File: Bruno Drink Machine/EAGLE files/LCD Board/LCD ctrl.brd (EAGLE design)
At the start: 88.2 x 81.2 mm, 38 parts, among them IC1 PIC24FJ256DA210-I/PT, IC2 IS62LV256AL, IC3 IS62LV256AL, IC4 BA3259H-HRP5, P1 CONN-40P-62684-401100ALF, P18 CONN-8P-PND, P2 USB-CON690-005-299-043

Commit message: made some of the changes; not all (will need to go through change list and confirm later)
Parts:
- moved U$32 78.4 mm to (5.08, 83.2), turned to 90 degrees
- moved U$35 78.4 mm to (76.2, 83.2), turned to 90 degrees
- moved U$33 71.1 mm to (5.08, 5.08), turned to 90 degrees
- moved U$34 71.1 mm to (76.2, 5.08), turned to 90 degrees
- moved P2 67.9 mm to (57.7, 85.5), turned to 180 degrees
- moved U$36 61.8 mm to (75.2, 14.0), turned to 90 degrees
- moved P18 57.6 mm to (74.2, 63.8), turned to 90 degrees
- moved P1 51.0 mm to (36.1, 76.4), turned to 180 degrees
- moved U$20 47.1 mm to (68.2, 22.0), turned to 90 degrees
- moved FET1 43.5 mm to (49.3, 70.1), turned to 0 degrees
- moved IC4 43.3 mm to (69.1, 52.0), turned to 270 degrees
- moved IC3 39.0 mm to (18.3, 24.4), turned to 180 degrees
- moved IC2 38.5 mm to (18.3, 56.1), turned to 180 degrees
- moved R2 34.2 mm to (60.2, 54.8), turned to 270 degrees
- moved ICSP1 32.6 mm to (59.2, 27.0), turned to 45 degrees
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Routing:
- net N$6: track 7.28 -> 6.56 mm
- net PGC: track 24.8 -> 24.2 mm
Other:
- board size 88.2 x 81.2 mm -> 81.2 x 88.2 mm

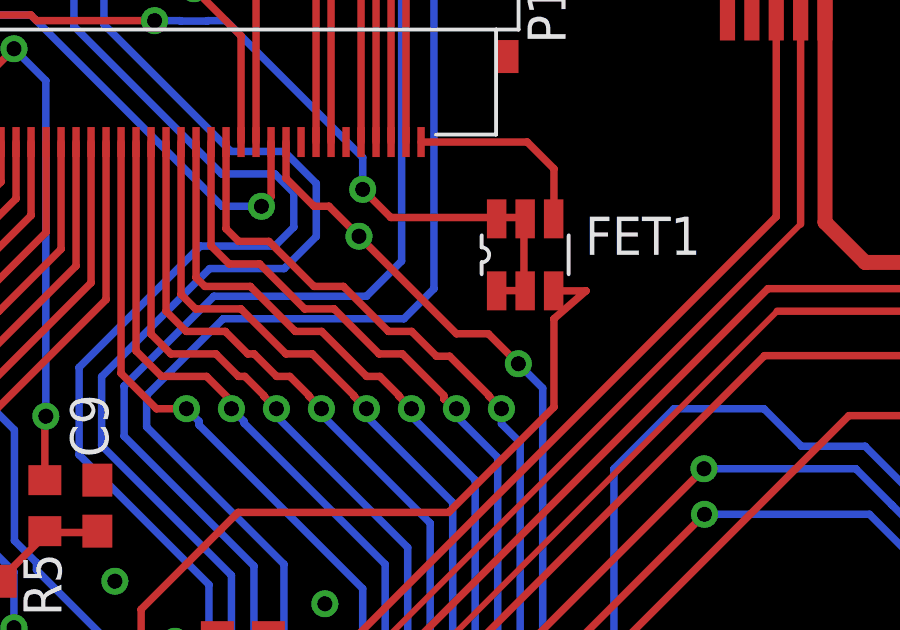
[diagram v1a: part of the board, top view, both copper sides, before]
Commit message: added another change (40p connector wrong) in change log; wrote some code
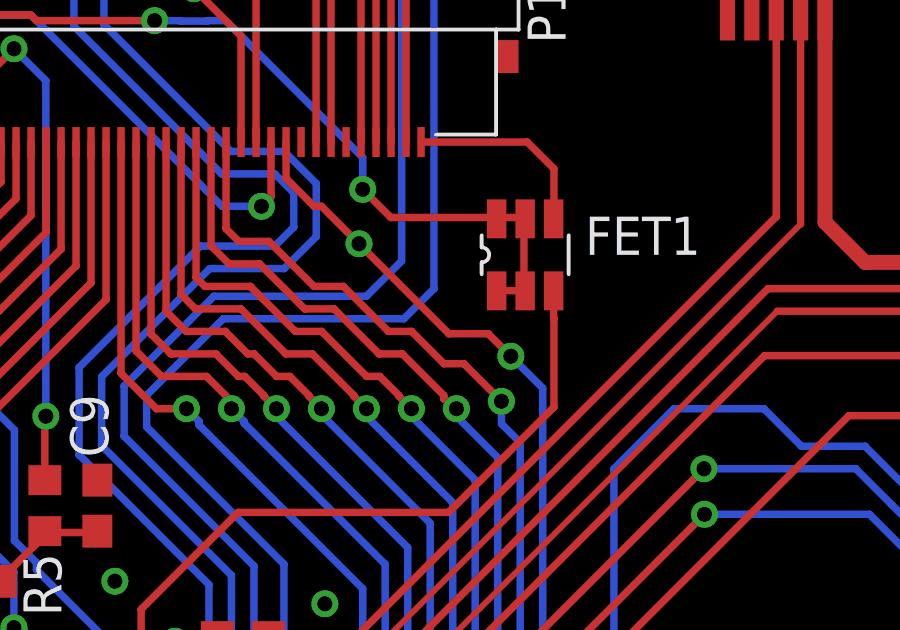
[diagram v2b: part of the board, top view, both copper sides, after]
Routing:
- net BACKLIGHT: track 28.8 -> 27.2 mm
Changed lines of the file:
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@@
 <wire x1="47.3282" y1="18.55339375" x2="47.3282" y2="18.6718" width="0.25" layer="1"/>
 <wire x1="47.3282" y1="18.6718" x2="47.6564" y2="19" width="0.25" layer="1"/>
-<via x="48.5" y="65" extent="1-16" drill="0.5"/>
-<wire x1="48.0782" y1="65.4218" x2="48.0782" y2="65.44660625" width="0.25" layer="1"/>
-<wire x1="48.0782" y1="65.4218" x2="48.5" y2="65" width="0.25" layer="1"/>
-<wire x1="48.5" y1="64.5" x2="48.5" y2="65" width="0.25" layer="16"/>
+<via x="48.5" y="65.25" extent="1-16" drill="0.5"/>
+<wire x1="48.5" y1="64.5" x2="48.5" y2="65.25" width="0.25" layer="16"/>
 <via x="28.75" y="44" extent="1-16" drill="0.5"/>
 <wire x1="47.6564" y1="19" x2="47.6564" y2="17.4064" width="0.25" layer="16"/>
@@
 <wire x1="49.125" y1="30.2434125" x2="49.125" y2="63.875" width="0.25" layer="16"/>
 <wire x1="49.125" y1="63.875" x2="48.5" y2="64.5" width="0.25" layer="16"/>
-<wire x1="48.0782" y1="65.44660625" x2="46.77480625" y2="66.75" width="0.25" layer="1"/>
 <wire x1="45.50726875" y1="67.5782" x2="44.7324625" y2="67.5782" width="0.25" layer="1"/>
-<wire x1="46.77480625" y1="66.75" x2="46.33546875" y2="66.75" width="0.25" layer="1"/>
-<wire x1="46.33546875" y1="66.75" x2="45.50726875" y2="67.5782" width="0.25" layer="1"/>
+<wire x1="46.58546875" y1="66.5" x2="45.50726875" y2="67.5782" width="0.25" layer="1"/>
 <wire x1="44.7324625" y1="67.5782" x2="43.2324625" y2="69.0782" width="0.25" layer="1"/>
 <wire x1="43.2324625" y1="69.0782" x2="42.24991875" y2="69.0782" width="0.25" layer="1"/>
@@
 <wire x1="39.32" y1="73.89" x2="39.32" y2="71" width="0.25" layer="1"/>
 <wire x1="39.32" y1="71" x2="39.7418" y2="70.5782" width="0.25" layer="1"/>
+<wire x1="48.5" y1="65.25" x2="47.25" y2="66.5" width="0.25" layer="1"/>
+<wire x1="47.25" y1="66.5" x2="46.58546875" y2="66.5" width="0.25" layer="1"/>
 </signal>
 <signal name="DB1">
@@
 <contactref element="P1" pad="31"/>
 <wire x1="41.32" y1="73.89" x2="41.32" y2="72.68" width="0.25" layer="1"/>
-<via x="43.75" y="70.75" extent="1-16" drill="0.5"/>
+<via x="43.75" y="70.5" extent="1-16" drill="0.5"/>
 <wire x1="41.32" y1="72.68" x2="42.25" y2="71.75" width="0.25" layer="1"/>
-<wire x1="42.25" y1="71.75" x2="42.75" y2="71.75" width="0.25" layer="1"/>
-<wire x1="42.75" y1="71.75" x2="43.75" y2="70.75" width="0.25" layer="1"/>
+<wire x1="42.25" y1="71.75" x2="42.5" y2="71.75" width="0.25" layer="1"/>
+<wire x1="42.5" y1="71.75" x2="43.75" y2="70.5" width="0.25" layer="1"/>
 <wire x1="42.88" y1="39.29" x2="42.88" y2="36.0593375" width="0.2" layer="1"/>
 <wire x1="50.141" y1="28.7983375" x2="50.141" y2="28.33419375" width="0.25" layer="1"/>
 <via x="50.141" y="28.33419375" extent="1-16" drill="0.5"/>
 <wire x1="42.88" y1="36.0593375" x2="50.141" y2="28.7983375" width="0.2" layer="1"/>
-<wire x1="47" y1="67.5" x2="43.75" y2="70.75" width="0.25" layer="1"/>
-<wire x1="47" y1="67.5" x2="48.0625" y2="67.5" width="0.25" layer="1"/>
-<wire x1="49.0625" y1="66.5" x2="48.0625" y2="67.5" width="0.25" layer="1"/>
-<wire x1="49.875" y1="65.6875" x2="49.0625" y2="66.5" width="0.25" layer="16"/>
+<wire x1="46.75" y1="67.5" x2="43.75" y2="70.5" width="0.25" layer="1"/>
+<wire x1="46.75" y1="67.5" x2="48.0625" y2="67.5" width="0.25" layer="1"/>
+<wire x1="48.8125" y1="66.75" x2="48.0625" y2="67.5" width="0.25" layer="1"/>
+<wire x1="49.875" y1="65.6875" x2="48.8125" y2="66.75" width="0.25" layer="16"/>
 <wire x1="49.875" y1="28.625" x2="49.875" y2="65.6875" width="0.25" layer="16"/>
 <wire x1="50.0625" y1="28.4375" x2="49.875" y2="28.625" width="0.25" layer="16"/>
 <wire x1="50.0625" y1="28.4375" x2="50.141" y2="28.33419375" width="0.25" layer="16"/>
-<via x="49.0625" y="66.5" extent="1-16" drill="0.5"/>
+<via x="48.8125" y="66.75" extent="1-16" drill="0.5"/>
 </signal>
 <signal name="RST">
@@
 <contactref element="IC1" pad="67"/>
 <contactref element="FET1" pad="3"/>
-<wire x1="50.24" y1="68.93" x2="51.32" y2="68.93" width="0.25" layer="1"/>
-<wire x1="50.25" y1="68" x2="51.32" y2="68.93" width="0.25" layer="1"/>
 <wire x1="50.25" y1="65.0533125" x2="50.25" y2="68" width="0.25" layer="1"/>
 <wire x1="39.72111875" y1="61.545" x2="46.7416875" y2="61.545" width="0.25" layer="1"/>
@@
 <wire x1="39.28" y1="52.69" x2="39.28" y2="53.7806625" width="0.2" layer="1"/>
 <wire x1="39.28" y1="53.7806625" x2="36.48905625" y2="56.57160625" width="0.25" layer="1"/>
+<wire x1="50.25" y1="68" x2="50.24" y2="68.01" width="0.25" layer="1"/>
+<wire x1="50.24" y1="68.01" x2="50.24" y2="68.93" width="0.25" layer="1"/>
 </signal>
 </signals>
